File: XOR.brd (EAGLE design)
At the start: 100 x 50.8 mm, 63 parts, among them IC1 40106D, IC2 4030D, IC3 4520D, IC7 TL074D

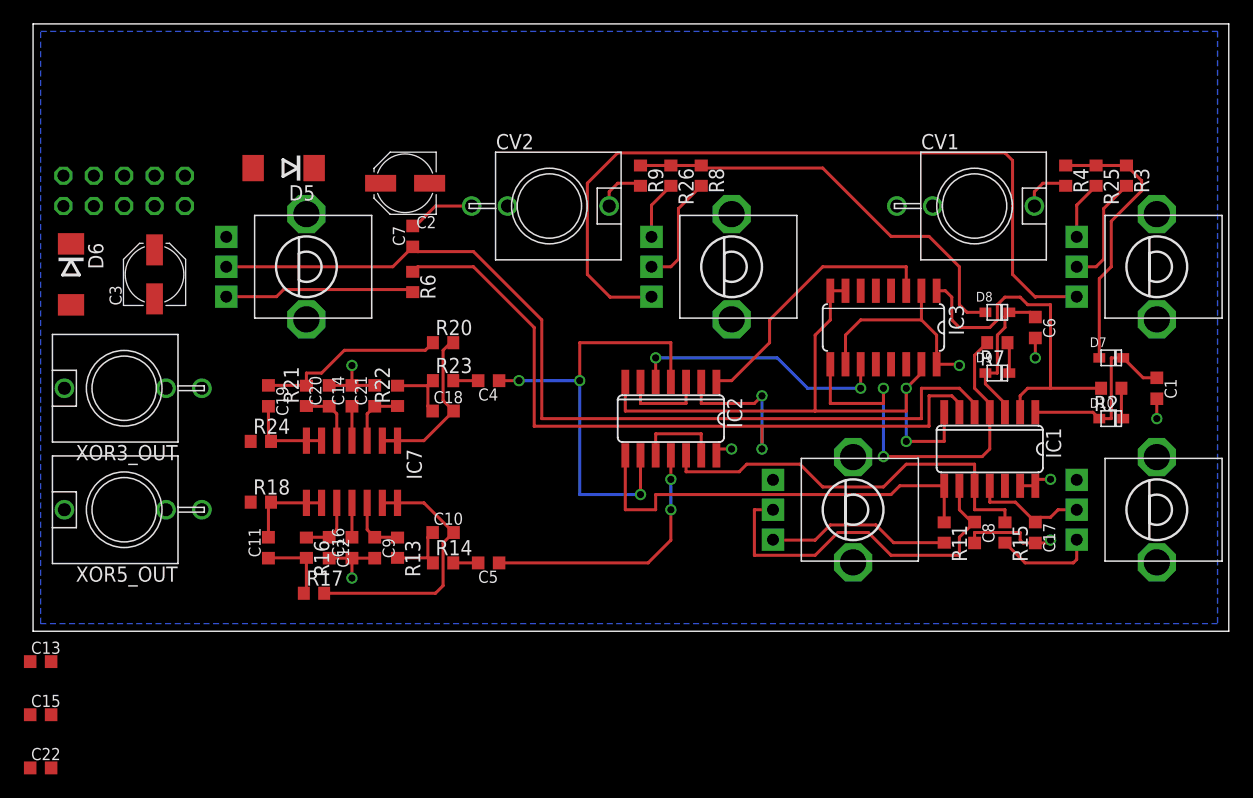
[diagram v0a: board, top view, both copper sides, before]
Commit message: Changed PSU diode type/footprint. Not fits DO214 package types. PCB: moved ICs a bit, better fit for CV in jack 1.
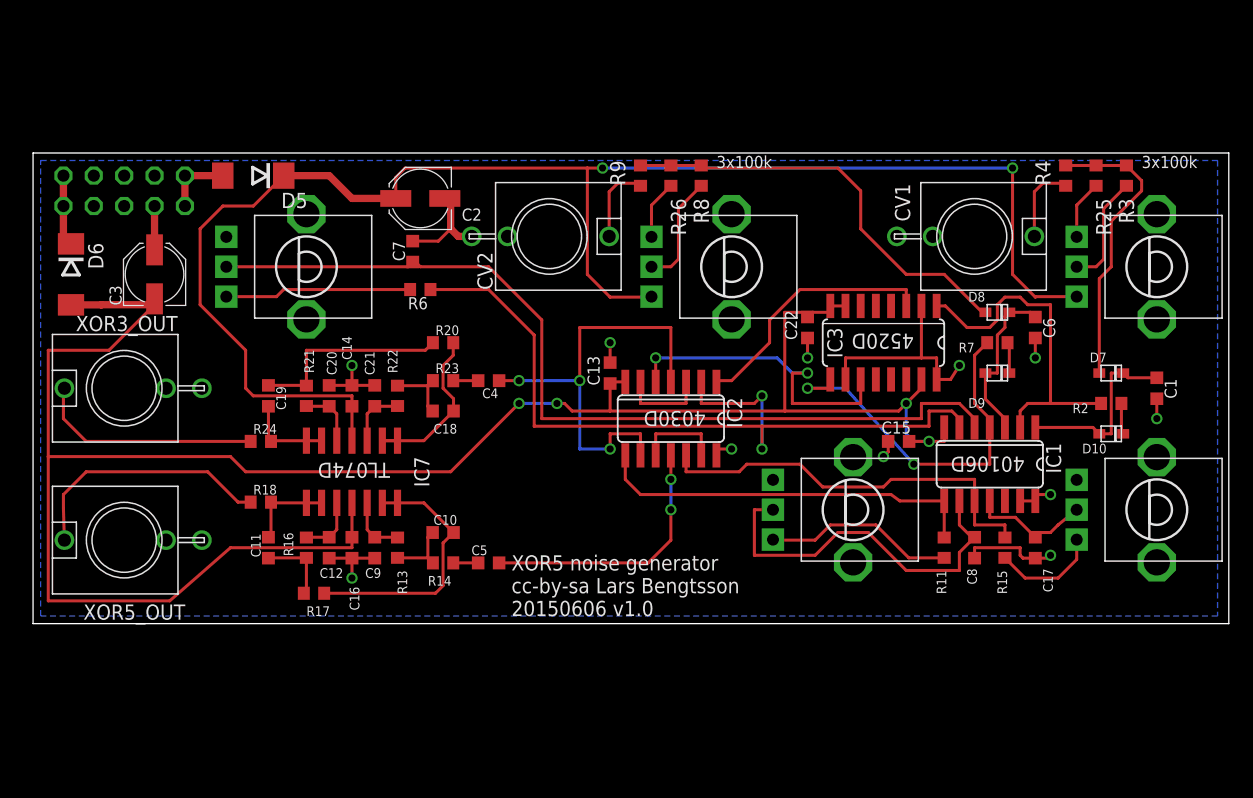
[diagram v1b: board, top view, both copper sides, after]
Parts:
- D5, D6: value 1N4148 -> 1N4004
- moved C15 75.3 mm to (72.4, 15.9)
- moved C22 74.0 mm to (64.8, 25.4), turned to 90 degrees
- moved C13 53.4 mm to (48.3, 21.6), turned to 270 degrees
- moved D5 2.62 mm to (18.4, 38.1)
- moved XOR5_OUT 2.54 mm to (7.62, 7.62)
- moved CV1 2.54 mm to (78.7, 33.0)
- moved CV2 2.54 mm to (43.2, 33.0)
- moved C2 1.80 mm to (32.4, 36.2)
- moved C7 1.27 mm to (31.8, 31.8)
- moved C17 1.27 mm to (83.8, 6.99)
- moved C8 1.27 mm to (78.7, 6.99)
- moved R11 1.27 mm to (76.2, 6.99)
- moved R15 1.27 mm to (81.3, 6.99)
- moved D10 1.27 mm to (90.2, 16.5)
- moved D7 1.27 mm to (90.2, 21.6)
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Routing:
- net -12V: track 55.2 -> 174.5 mm, vias 2 -> 4
- net +12V: track 69.2 -> 130.6 mm, vias 0 -> 2
- net N$23: track 0.00 -> 21.3 mm
- net N$37: track 0.00 -> 19.0 mm
- net GND: track 60.8 -> 72.3 mm, vias 8 -> 11
- net N$8: track 0.00 -> 5.97 mm
- net N$9: track 0.00 -> 5.71 mm
- net VCO_SQUARE2: track 22.2 -> 26.8 mm
- net SQUARE3: track 73.6 -> 69.2 mm
- net SQUARE4: track 35.9 -> 32.4 mm
- net N$2: track 4.20 -> 6.74 mm
- net N$19: track 4.20 -> 6.74 mm
- net N$14: track 77.9 -> 75.5 mm
- net VCO2_PULSE: track 33.7 -> 31.8 mm
- net XOR_MIX_3: track 38.7 -> 37.2 mm
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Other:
- board size 100 x 50.8 mm -> 100 x 39.4 mm
- board text added: "3x100k"
- board text added: "PSU"
- board text added: "RED STRIPE -12V ->"
- board text added: "XOR5"
- board text added: "XOR5 noise generator cc-by-sa 2015 Lars Bengtsson"
- board text added: "XOR5 noise generator cc-by-sa Lars Bengtsson 20150606 v1.0"

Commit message: Changed order in which oscillators are XORed together. Use bigger footprint for PSU smoothing caps. Moved XOR IC a bit & rerouted.
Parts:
- C2, C3: device rcl:PANASONIC_C -> rcl:PANASONIC_D
- moved C13 9.38 mm to (43.8, 13.3), turned to 0 degrees
- moved IC2 8.26 mm to (50.2, 10.2)
- moved C3 1.42 mm to (8.89, 30.5), turned to 0 degrees
- moved C22 1.27 mm to (64.8, 26.7)
- moved C7 1.27 mm to (33.0, 31.8), turned to 0 degrees
- moved D6 1.27 mm to (1.91, 29.8)
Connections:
- net N$10: now also IC2.3, IC2.9; no longer IC2.10, IC2.13
- net N$25: now also IC2.13, IC2.4; no longer IC2.3, IC2.6
- net SQUARE3: now also IC2.8; no longer IC2.2
- net SQUARE4: now also IC2.6; no longer IC2.8
- net VCO_SQUARE1: now also IC2.5; no longer IC2.1
- net VCO_SQUARE2: now also IC2.1; no longer IC2.5
- net XOR_MIX_3: now also IC2.11, IC2.2; no longer IC2.4, IC2.9
- net XOR_MIX_5: now also IC2.10; no longer IC2.11
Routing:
- net SQUARE4: track 32.4 -> 49.5 mm, vias 0 -> 2
- net VCO_SQUARE1: track 21.6 -> 37.5 mm, vias 0 -> 2
- net XOR_MIX_3: track 37.2 -> 25.7 mm, vias 3 -> 0
- net XOR_MIX_5: track 22.2 -> 11.3 mm, vias 2 -> 0
- net N$25: track 7.42 -> 17.9 mm, vias 0 -> 2
- net VCO2_PULSE: track 31.8 -> 24.2 mm, vias 2 -> 0
- net +12V: track 130.6 -> 125.1 mm
- net SQUARE5: track 34.2 -> 39.3 mm
- net N$14: track 75.5 -> 71.3 mm
- net VCO_SQUARE2: track 26.8 -> 23.0 mm
- net -12V: track 174.5 -> 177.5 mm
- net GND: track 72.3 -> 75.3 mm, vias 11 -> 12
- net SQUARE3: track 69.2 -> 71.4 mm
- net N$17: track 35.8 -> 33.9 mm
- net N$24: track 10.2 -> 11.9 mm

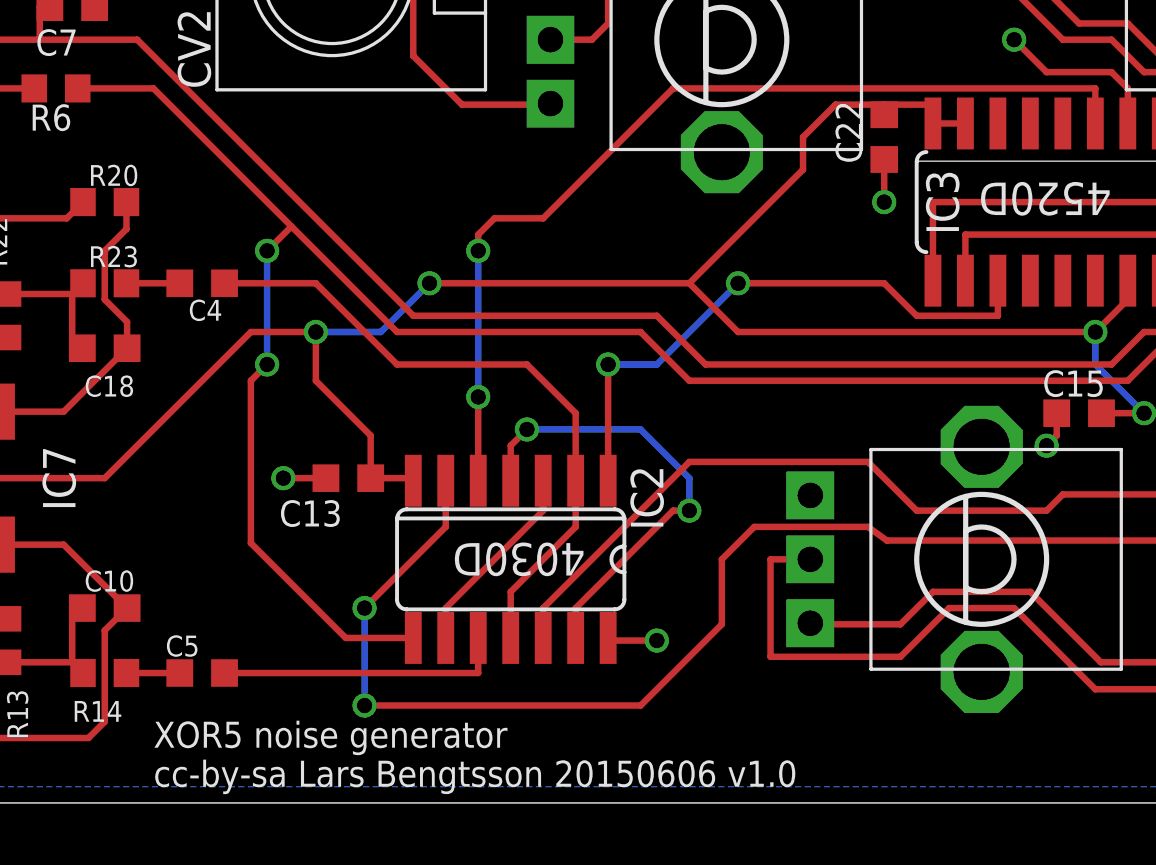
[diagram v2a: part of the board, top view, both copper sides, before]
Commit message: Added 2x10k resistors that pulls the filter inputs to ground (got DC offset problem on the filter outputs without them).
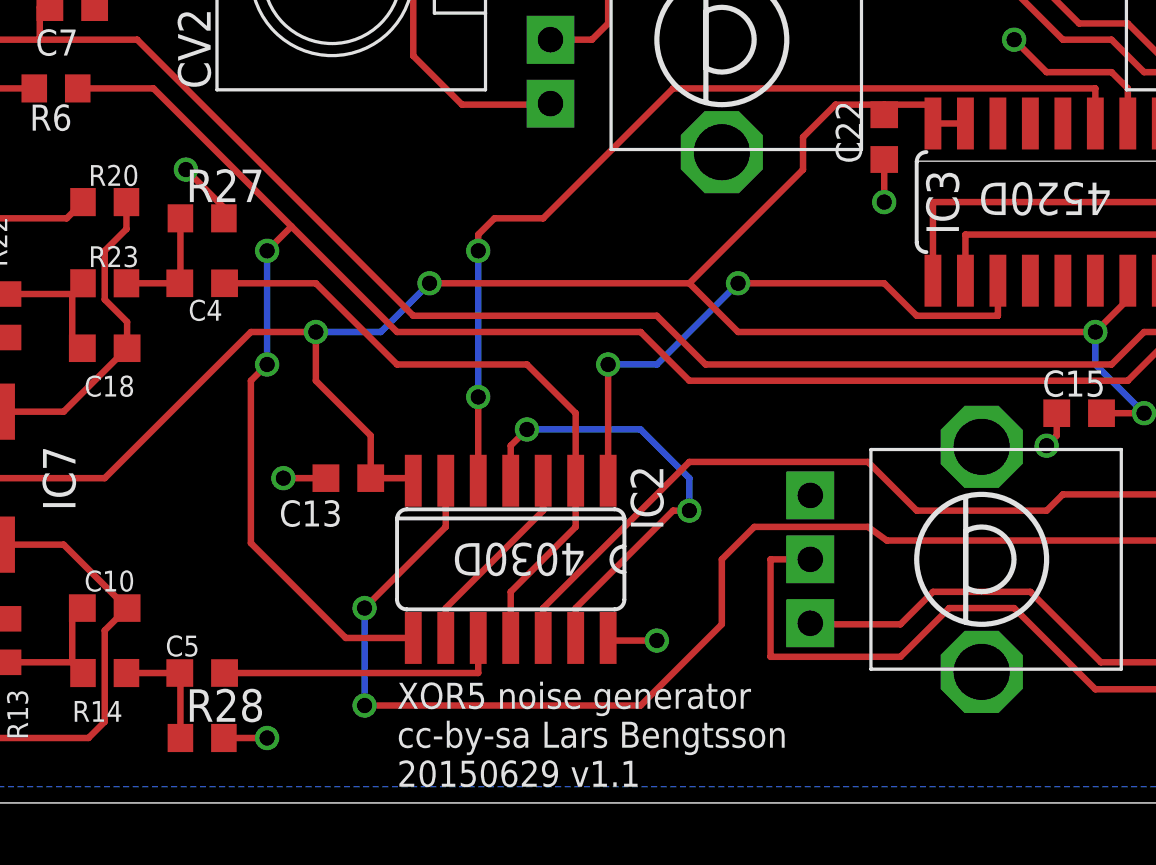
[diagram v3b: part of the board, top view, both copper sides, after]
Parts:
- added R27, R28: 10k, rcl:R0603
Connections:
- net GND: now also R27.2, R28.2
- net N$33: now also R27.1
- net N$38: now also R28.1
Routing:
- net GND: track 75.3 -> 79.5 mm, vias 12 -> 14
- net N$33: track 2.09 -> 4.64 mm
- net N$38: track 2.09 -> 4.64 mm
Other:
- board text added: "XOR5 noise generator cc-by-sa Lars Bengtsson 20150629 v1.1"
- board text removed: "XOR5 noise generator cc-by-sa Lars Bengtsson 20150606 v1.0"
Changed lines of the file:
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@@
 <text x="57.15" y="38.735" size="1.016" layer="25" font="vector">3x100k</text>
 <text x="92.71" y="38.735" size="1.016" layer="25" font="vector">3x100k</text>
-<text x="36.195" y="1.27" size="1.016" layer="25" font="vector">XOR5 noise generator
-cc-by-sa Lars Bengtsson 20150606 v1.0</text>
+<text x="45.72" y="1.27" size="1.016" layer="25" font="vector">XOR5 noise generator
+cc-by-sa Lars Bengtsson
+20150629 v1.1</text>
 <text x="6.985" y="5.715" size="1.016" layer="26" font="vector" rot="MR90">XOR5 noise generator
 cc-by-sa 2015 Lars Bengtsson</text>
@@
 <attribute name="VALUE" x="62.61" y="25.235" size="1.016" layer="27" rot="R90"/>
 </element>
+<element name="R27" library="rcl" package="R0603" value="10k" x="38.1" y="23.495"/>
+<element name="R28" library="rcl" package="R0603" value="10k" x="38.1" y="3.175"/>
 </elements>
 <signals>
@@
 <wire x1="10.16" y1="35.56" x2="10.16" y2="30.48" width="0.6096" layer="1"/>
 <wire x1="10.16" y1="30.48" x2="11.29" y2="30.48" width="0.6096" layer="1"/>
+<contactref element="R27" pad="2"/>
+<contactref element="R28" pad="2"/>
+<wire x1="38.95" y1="3.175" x2="40.64" y2="3.175" width="0.254" layer="1"/>
+<via x="40.64" y="3.175" extent="1-16" drill="0.6" shape="square"/>
+<via x="37.465" y="25.4" extent="1-16" drill="0.6" shape="square"/>
+<wire x1="38.95" y1="23.495" x2="38.95" y2="23.915" width="0.254" layer="1"/>
+<wire x1="38.95" y1="23.915" x2="37.465" y2="25.4" width="0.254" layer="1"/>
 </signal>
 <signal name="N$1">
@@
 <contactref element="R23" pad="2"/>
 <wire x1="35.14" y1="20.955" x2="37.225" y2="20.955" width="0.254" layer="1"/>
+<contactref element="R27" pad="1"/>
+<wire x1="37.25" y1="23.495" x2="37.25" y2="20.98" width="0.254" layer="1"/>
+<wire x1="37.25" y1="20.98" x2="37.225" y2="20.955" width="0.254" layer="1"/>
 </signal>
 <signal name="N$38">
@@
 <contactref element="C5" pad="2"/>
 <wire x1="35.14" y1="5.715" x2="37.225" y2="5.715" width="0.254" layer="1"/>
+<contactref element="R28" pad="1"/>
+<wire x1="37.25" y1="3.175" x2="37.25" y2="5.69" width="0.254" layer="1"/>
+<wire x1="37.25" y1="5.69" x2="37.225" y2="5.715" width="0.254" layer="1"/>
 </signal>
 <signal name="N$11">
